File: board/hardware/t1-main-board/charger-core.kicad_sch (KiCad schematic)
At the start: 29 parts, among them U601 BQ25798RQMR

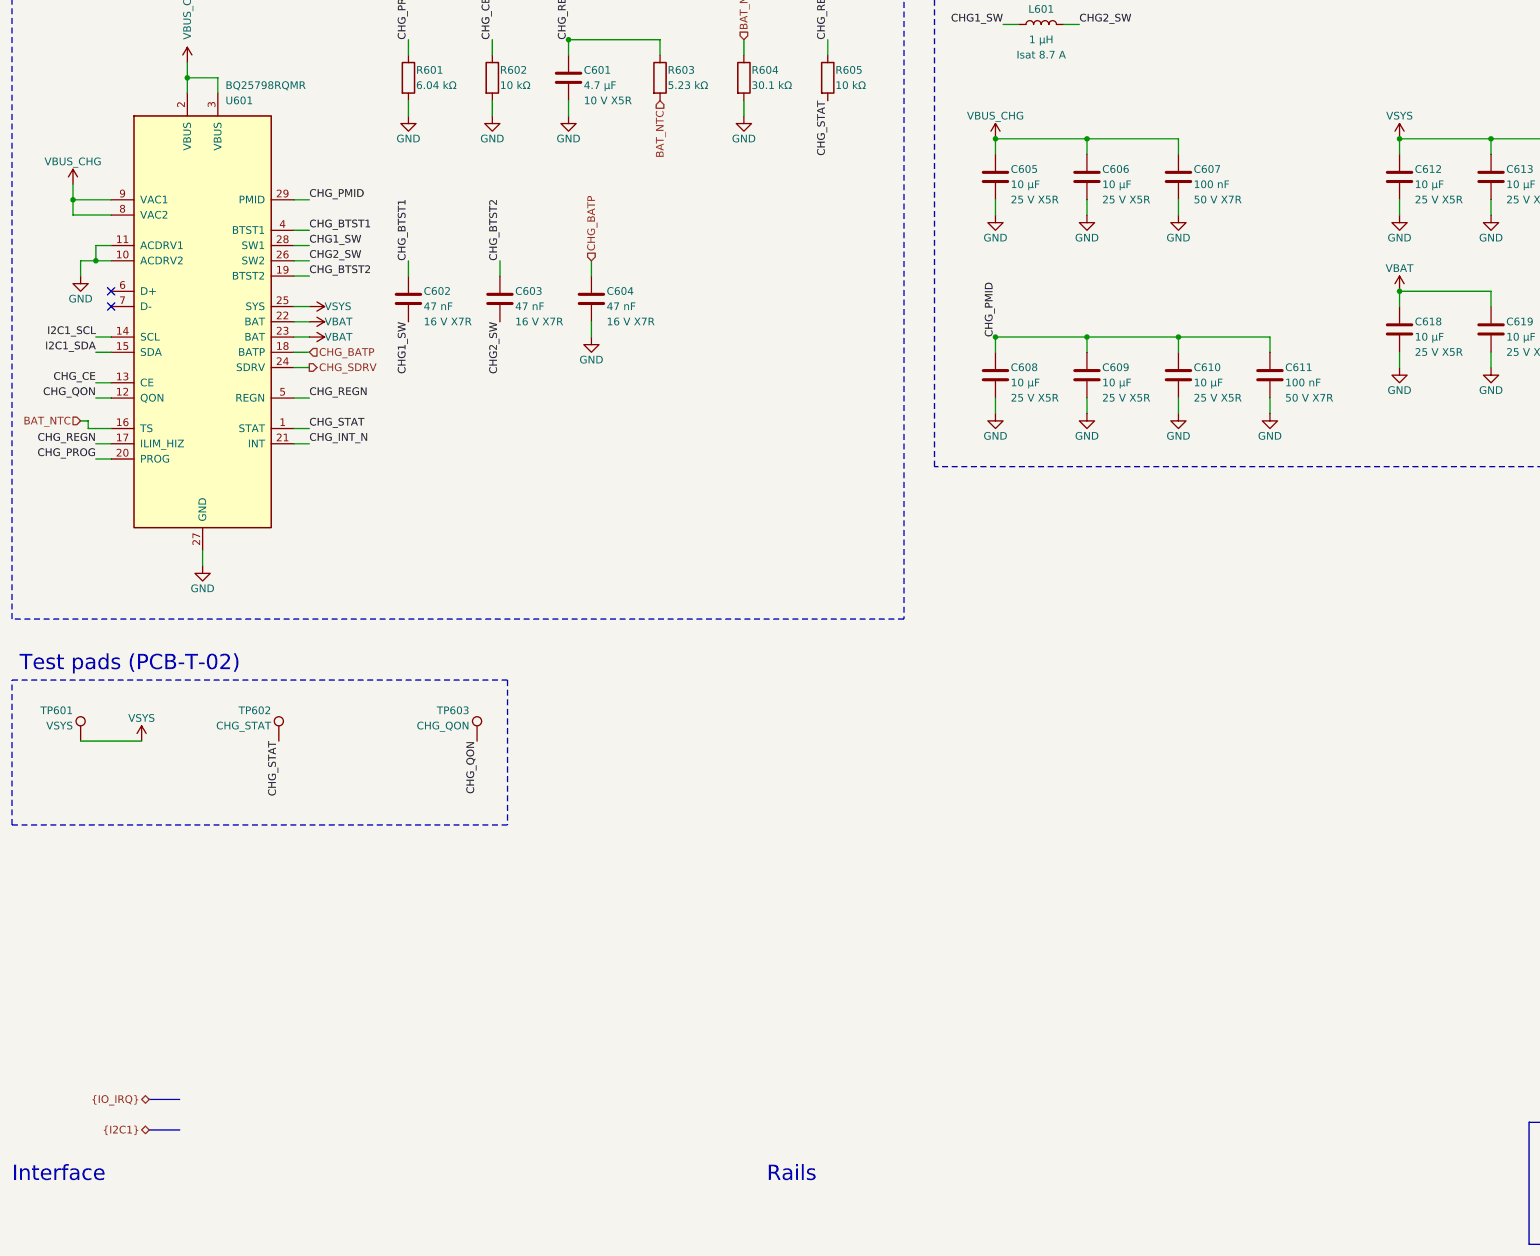
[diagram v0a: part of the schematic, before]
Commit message: Board: capture blk.current-monitors
Five INA236 on I2C1 (0x40-0x43, 0x48) with their shunts, per power tree
§4.12 and BOM v1 lines 54 and 136. The measured branches are rails of
their own (VSYS_SRC, VSYS_LV_AUDIO, VSYS_AUDIO, VSYS_LV_BL, VSYS_P5V1),
fed through the shunts on this sheet; the charger, audio, backlight and
5.1 V sheets take them. The root's layout may leave a stack level empty,
so the block sits under the notes; IC bboxes hold turned rail values;
passive rows hold a bottom rail's text.

Co-Authored-By: Claude Opus 5.5 <noreply@anthropic.com>
Claude-Session: https://claude.ai/code/session_01Ei262h3TpgY9vyfNLMi5Mn
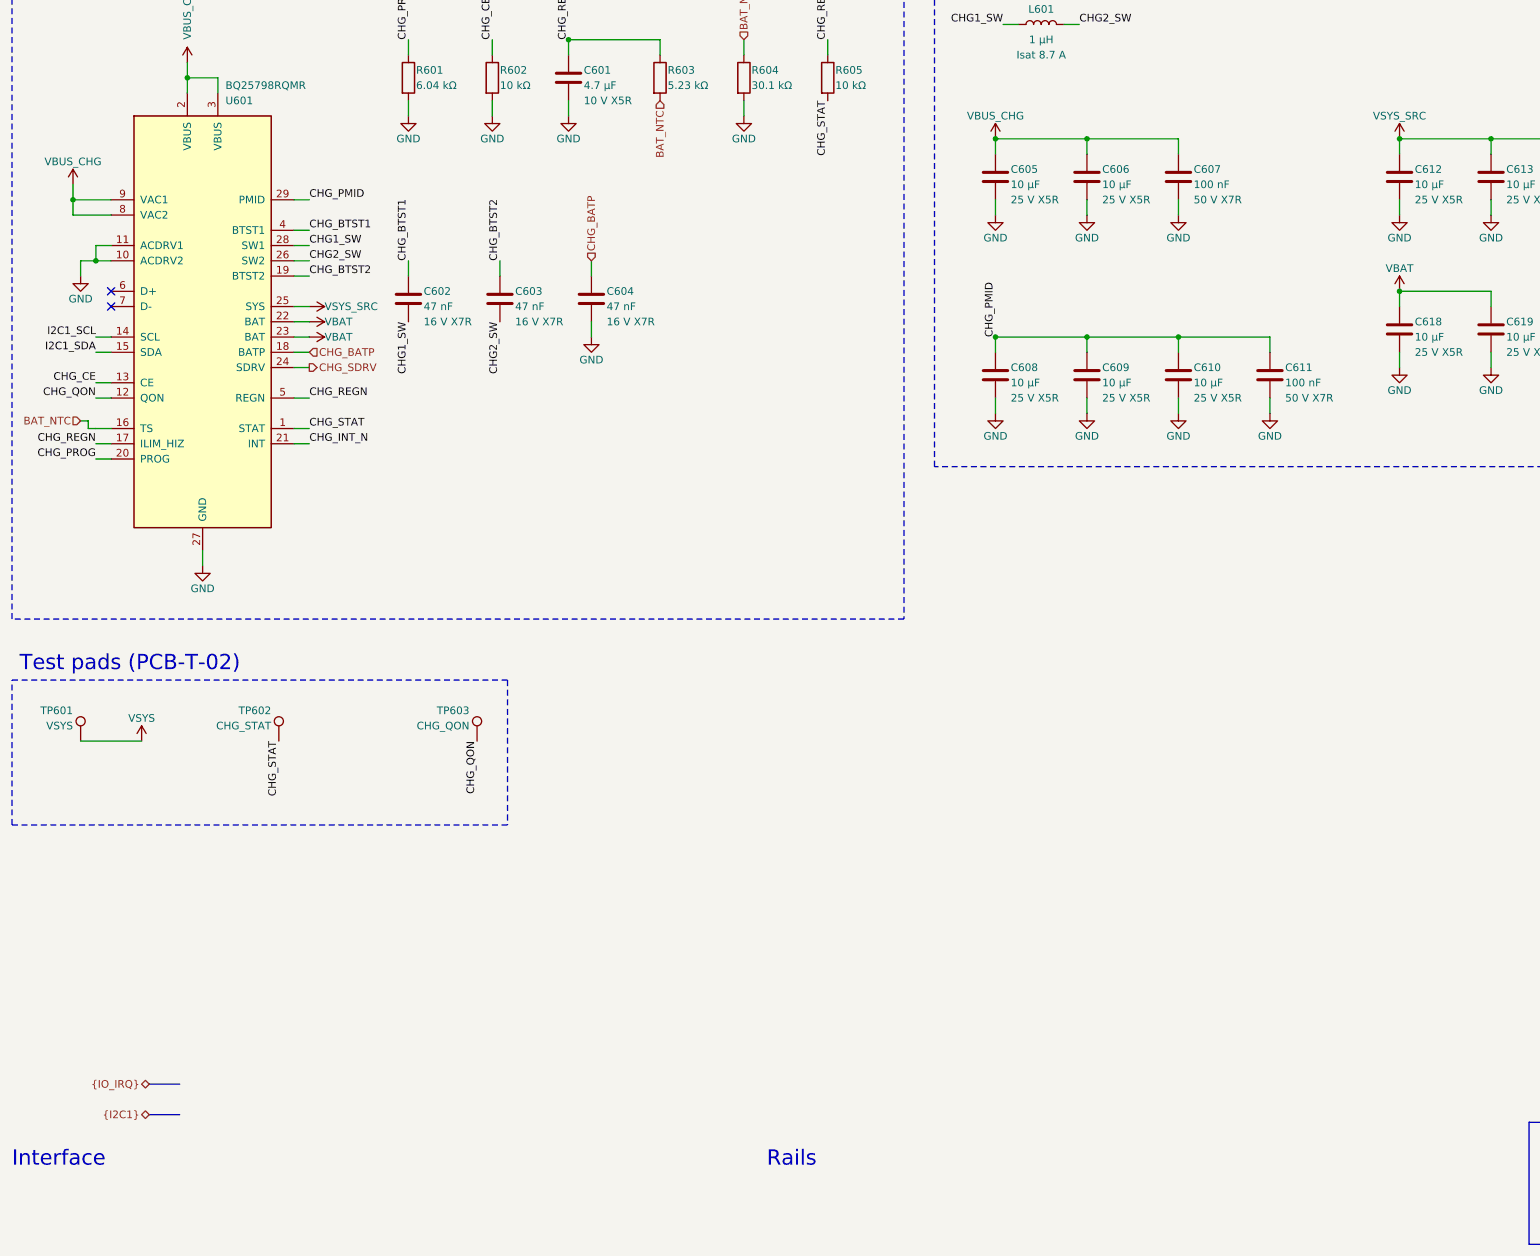
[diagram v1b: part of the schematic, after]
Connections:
- net VSYS: no longer C612.1, C613.1, C614.1, C615.1, C616.1, C617.1, U601.25 (SYS)
- new net VSYS_SRC: C612.1, C613.1, C614.1, C615.1, C616.1, C617.1, U601.25 (SYS)

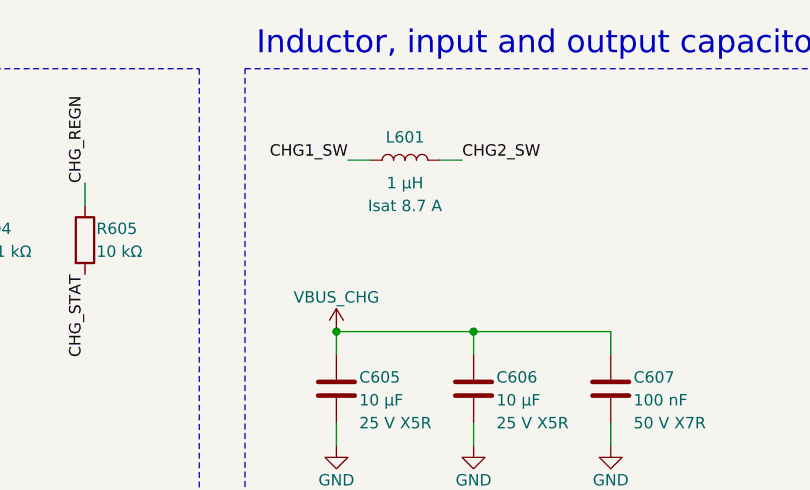
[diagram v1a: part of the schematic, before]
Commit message: Compaction: lower inductors, 0201 decoupling, 0.8 mm signal test pads
A matrix tool (hardware/studies/compaction) checks each candidate against
the design's stresses: same inductance, design peak <= 70 % and the
converter's maximum limit <= 100 % of Isat (30 % drop), height zones,
ratings at least twice the rail, PCB-D-06; sourcing outcome per part.

Applied (placement v1 decision 12, BOM v1.15):
- L601, L4401: XGL4015-102MEC (1.5 mm) for XAL/XGL4020-102MEC (2.1 mm);
- L1001, L5101: XGL4015-471MEC (1.5 mm) for Wurth 744373240047, on the
  stock XxL4020 land (the Wurth land was never drawn);
- L1201 is 1.2 mm (XGL4012, per-MPN heights): it moves next to the SoC;
- 58 x 100 nF decoupling on rails <= 3.3 V in core/IO/radio: 0201;
- 51 test pads on signal nets: 0.8 mm (PCB-D-06 v0.16, JLCPCB guide).
Kept: L901, L2802 (XGL4015 at 103 % of Isat at the limit); no thinner
0805/1206 capacitor passes (obsolete, NRND or unlisted).

Board need 113 % -> 111 % (core band 227 -> 203 %, power band 258 ->
233 %, radio band 19 -> 0 %); only C904 still relies on PCB-Z-04.
ERC 0 errors, craft Q1 met, DRC 0 errors (605 warnings), pcb and study
tests pass, rules test board PASS.

Co-Authored-By: Claude Opus 5.5 <noreply@anthropic.com>
Claude-Session: https://claude.ai/code/session_01Ei262h3TpgY9vyfNLMi5Mn
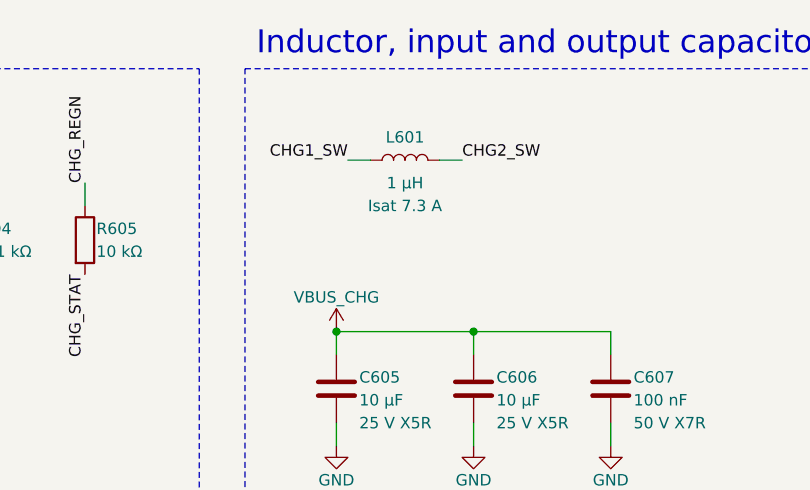
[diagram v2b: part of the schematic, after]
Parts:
- L601: MPN XAL4020-102MEC -> XGL4015-102MEC; MPN_2 XGL4020-102MEC -> XGL4012-102MEC; Second_Source Coilcraft XGL4020-102MEC (same land, BOM v1 line 40) -> Coilcraft XGL4012-102MEC (same land, 1.2 mm, Isat 6.6 A at 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; Spec Isat 8.7 A -> Isat 7.3 A
- TP602, TP603: footprint TestPoint:TestPoint_Pad_D1.0mm -> T1_Main_Board:TestPoint_Pad_D0.8mm
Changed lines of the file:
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@@
   (property "Reference" "L601" (at 194.31 43.18 90) (effects (font (size 1.27 1.27))))
   (property "Value" "1 µH" (at 194.31 48.26 90) (effects (font (size 1.27 1.27))))
-  (property "Spec" "Isat 8.7 A" (at 194.31 50.8 90) (effects (font (size 1.27 1.27))))
+  (property "Spec" "Isat 7.3 A" (at 194.31 50.8 90) (effects (font (size 1.27 1.27))))
   (property "Footprint" "Inductor_SMD:L_Coilcraft_XxL4020" (at 194.31 45.72 0) (effects (font (size 1.27 1.27))) (hide yes))
-  (property "Datasheet" "https://www.coilcraft.com/getmedia/6adcb47d-8b55-416c-976e-1e22e0d2848c/xal4000.pdf" (at 194.31 45.72 0) (effects (font (size 1.27 1.27))) (hide yes))
-  (property "Description" "Power inductor, 1.0 uH 20 %, Isat 8.7 A (30 % drop), 4.0 x 4.0 x 2.1 mm" (at 194.31 45.72 0) (effects (font (size 1.27 1.27))) (hide yes))
+  (property "Datasheet" "https://coilcraft.com/getmedia/c5d04454-742d-473e-8b80-06c97338c587/xgl4015.pdf" (at 194.31 45.72 0) (effects (font (size 1.27 1.27))) (hide yes))
+  (property "Description" "Power inductor, 1.0 uH 20 %, Isat 7.3 A (30 % drop), Irms 6.5 A, 4.0 x 4.0 x 1.5 mm" (at 194.31 45.72 0) (effects (font (size 1.27 1.27))) (hide yes))
   (property "Manufacturer" "Coilcraft" (at 194.31 45.72 0) (effects (font (size 1.27 1.27))) (hide yes))
-  (property "MPN" "XAL4020-102MEC" (at 194.31 45.72 0) (effects (font (size 1.27 1.27))) (hide yes))
-  (property "Second_Source" "Coilcraft XGL4020-102MEC (same land, BOM v1 line 40)" (at 194.31 45.72 0) (effects (font (size 1.27 1.27))) (hide yes))
+  (property "MPN" "XGL4015-102MEC" (at 194.31 45.72 0) (effects (font (size 1.27 1.27))) (hide yes))
+  (property "Second_Source" "Coilcraft XGL4012-102MEC (same land, 1.2 mm, Isat 6.6 A at 30 % drop)" (at 194.31 45.72 0) (effects (font (size 1.27 1.27))) (hide yes))
   (property "Manufacturer_2" "Coilcraft" (at 194.31 45.72 0) (effects (font (size 1.27 1.27))) (hide yes))
-  (property "MPN_2" "XGL4020-102MEC" (at 194.31 45.72 0) (effects (font (size 1.27 1.27))) (hide yes))
+  (property "MPN_2" "XGL4012-102MEC" (at 194.31 45.72 0) (effects (font (size 1.27 1.27))) (hide yes))
   (property "Block" "blk.charger-core" (at 194.31 45.72 0) (effects (font (size 1.27 1.27))) (hide yes))
   (pin "1")
@@
   (property "Reference" "TP602" (at 66.04 160.02 0) (effects (font (size 1.27 1.27)) (justify right)))
   (property "Value" "CHG_STAT" (at 66.04 162.56 0) (effects (font (size 1.27 1.27)) (justify right)))
-  (property "Footprint" "TestPoint:TestPoint_Pad_D1.0mm" (at 67.31 165.1 0) (effects (font (size 1.27 1.27))) (hide yes))
+  (property "Footprint" "T1_Main_Board:TestPoint_Pad_D0.8mm" (at 67.31 165.1 0) (effects (font (size 1.27 1.27))) (hide yes))
   (property "Datasheet" "~" (at 67.31 165.1 0) (effects (font (size 1.27 1.27))) (hide yes))
-  (property "Description" "Test pad, 1.0 mm" (at 67.31 165.1 0) (effects (font (size 1.27 1.27))) (hide yes))
+  (property "Description" "Test pad, 0.8 mm, signal net" (at 67.31 165.1 0) (effects (font (size 1.27 1.27))) (hide yes))
   (property "Block" "blk.charger-core" (at 67.31 165.1 0) (effects (font (size 1.27 1.27))) (hide yes))
   (pin "1")
@@
   (property "Reference" "TP603" (at 99.06 160.02 0) (effects (font (size 1.27 1.27)) (justify right)))
   (property "Value" "CHG_QON" (at 99.06 162.56 0) (effects (font (size 1.27 1.27)) (justify right)))
-  (property "Footprint" "TestPoint:TestPoint_Pad_D1.0mm" (at 100.33 165.1 0) (effects (font (size 1.27 1.27))) (hide yes))
+  (property "Footprint" "T1_Main_Board:TestPoint_Pad_D0.8mm" (at 100.33 165.1 0) (effects (font (size 1.27 1.27))) (hide yes))
   (property "Datasheet" "~" (at 100.33 165.1 0) (effects (font (size 1.27 1.27))) (hide yes))
-  (property "Description" "Test pad, 1.0 mm" (at 100.33 165.1 0) (effects (font (size 1.27 1.27))) (hide yes))
+  (property "Description" "Test pad, 0.8 mm, signal net" (at 100.33 165.1 0) (effects (font (size 1.27 1.27))) (hide yes))
   (property "Block" "blk.charger-core" (at 100.33 165.1 0) (effects (font (size 1.27 1.27))) (hide yes))
   (pin "1")

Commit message: Board on libs v0.2.0: lower-case kebab vendor keys (HL-13)
The libs submodule moves to v0.2.0 (5f24483). Every library nickname in
the generator, the placement tool and the floorplan study follows the
key table (Texas_Instruments -> texas-instruments, OpenDAP_Device ->
opendap-generic, Rockchip and Rockchip_PMIC -> rockchip, ...); the
library tables are written from the files. Schematic and board
regenerated.

Checks: ERC 0 errors (warnings unchanged); DRC 0 errors, 605 warnings,
the same counts by type, schematic parity 0; every placement identical;
craft Q1 met; pcb tests pass; STEP export resolves every libs 3D model
(the 27 parts without a model are KiCad stock lands that have none).

Co-Authored-By: Claude Opus 5.5 <noreply@anthropic.com>
Claude-Session: https://claude.ai/code/session_01Ei262h3TpgY9vyfNLMi5Mn
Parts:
- U601: footprint Texas_Instruments:VQFN-HR-29_4x4mm_P0.4mm -> texas-instruments:VQFN-HR-29_4x4mm_P0.4mm; symbol Texas_Instruments:BQ25798RQMR -> texas-instruments:BQ25798RQMR
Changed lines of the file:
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@@
 (paper "A3")
 (title_block (title "Charger: BQ25798") (date "2026-10-25") (rev "A") (company "The OpenDAP Project") (comment 1 "blk.charger-core") (comment 2 "2S buck-boost charger, its inductor and capacitors; VSYS out"))
-(symbol (lib_id "Texas_Instruments:BQ25798RQMR") (at 54.61 95.25 0) (unit 1) (body_style 1) (exclude_from_sim no) (in_bom yes) (on_board yes) (dnp no)
+(symbol (lib_id "texas-instruments:BQ25798RQMR") (at 54.61 95.25 0) (unit 1) (body_style 1) (exclude_from_sim no) (in_bom yes) (on_board yes) (dnp no)
   (property "Reference" "U601" (at 58.42 58.42 0) (effects (font (size 1.27 1.27)) (justify left)))
   (property "Value" "BQ25798RQMR" (at 58.42 55.88 0) (effects (font (size 1.27 1.27)) (justify left)))
-  (property "Footprint" "Texas_Instruments:VQFN-HR-29_4x4mm_P0.4mm" (at 54.61 95.25 0) (effects (font (size 1.27 1.27))) (hide yes))
+  (property "Footprint" "texas-instruments:VQFN-HR-29_4x4mm_P0.4mm" (at 54.61 95.25 0) (effects (font (size 1.27 1.27))) (hide yes))
   (property "Datasheet" "https://www.ti.com/lit/ds/symlink/bq25798.pdf" (at 54.61 95.25 0) (effects (font (size 1.27 1.27))) (hide yes))
   (property "Description" "I2C-controlled 1-4 cell 5 A buck-boost battery charger with NVDC power path, dual-input selector, MPPT and backup mode, VQFN-HR-29 (RQM) 4 x 4 mm" (at 54.61 95.25 0) (effects (font (size 1.27 1.27))) (hide yes))
